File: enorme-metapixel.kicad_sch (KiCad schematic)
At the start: 15 parts, among them J1 VIN, J2 STRIP_0, J3 STRIP_1, J4 STRIP_2, J5 UART, SW1 SW_RESET, SW2 SW_BOOT, U1 BD33FC0FP, U2 ESP32-WROOM-32

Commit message: Rev 2
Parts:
- added D2: Ch.0, ENSADLED:ARGB_0404, symbol Device:LED_ARGB
- added D3: Ch.1, ENSADLED:ARGB_0404, symbol Device:LED_ARGB
- added D4: Ch.2, ENSADLED:ARGB_0404, symbol Device:LED_ARGB
- added H1: M4, MountingHole:MountingHole_4.3mm_M4, symbol Mechanical:MountingHole
- added H2: PEG, MountingHole:MountingHole_3.2mm_M3, symbol Mechanical:MountingHole
- added R22, R23, R24, R25, R26, R27, R28, R29, R30: 3.3k, Resistor_SMD:R_0603_1608Metric, symbol Device:R_Small
- J1: footprint TerminalBlock:TerminalBlock_bornier-2_P5.08mm -> ENSADLED:fiche_bornier-2_P5.08mm
- J2, J3, J4: footprint TerminalBlock:TerminalBlock_bornier-4_P5.08mm -> ENSADLED:fiche-bornier-4_P5.08mm
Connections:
- net VCC: now also D2.1 (A), D3.1 (A), D4.1 (A)
- net ch0_0: now also R23.1
- net ch0_1: now also R22.1
- net ch0_2: now also R24.1
- net ch1_0: now also R26.1
- net ch1_1: now also R25.1
- net ch1_2: now also R27.1
- net ch2_0: now also R29.1
- net ch2_1: now also R28.1
- net ch2_2: now also R30.1
- net ledc6: now reaches U2.12 (IO27)
- net ledc7: now reaches U2.13 (IO14)
- net ledc8: now reaches U2.14 (IO12)
- net ledc3: now reaches U2.26 (IO4)
- net ledc0: now reaches U2.29 (IO5)
- net IO15: no longer names the net of U2.23 (IO15)
- net IO16 renamed ledc4
- net IO17 renamed ledc5
- net IO18 renamed ledc1
- net IO19 renamed ledc2
- net IO21: no longer names the net of U2.33 (IO21)
- net IO22: no longer names the net of U2.36 (IO22)
- net IO23: no longer names the net of U2.37 (IO23)
- net IO25: no longer names the net of U2.10 (IO25)
- new net: D3.2 (RK), R25.2
- new net: D4.4 (BK), R30.2
- new net: D2.4 (BK), R24.2
- new net: D3.4 (BK), R27.2
- new net: D3.3 (GK), R26.2
- new net: D2.2 (RK), R22.2
- new net: D2.3 (GK), R23.2
- new net: D4.2 (RK), R28.2
- new net: D4.3 (GK), R29.2
- no-connect marks 0 -> 8

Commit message: Fix color order
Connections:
- net ch0_0: now also R24.1; no longer R23.1
- net ch0_2: now also R23.1; no longer R24.1
- net ch1_0: now also R27.1; no longer R26.1
- net ch1_2: now also R26.1; no longer R27.1
- net ch2_0: now also R30.1; no longer R29.1
- net ch2_2: now also R29.1; no longer R30.1
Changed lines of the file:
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@@
     (effects (font (size 0.8 0.8)) (justify right bottom))
   )
-  (label "ch0_2" (at 38.1 137.795 0) (fields_autoplaced)
+  (label "ch0_2" (at 38.1 132.715 0) (fields_autoplaced)
     (effects (font (size 0.8 0.8)) (justify left bottom))
   )
@@
     (effects (font (size 0.8 0.8)) (justify left bottom))
   )
-  (label "ch2_0" (at 38.1 178.435 0) (fields_autoplaced)
+  (label "ch2_0" (at 38.1 183.515 0) (fields_autoplaced)
     (effects (font (size 0.8 0.8)) (justify left bottom))
   )
@@
     (effects (font (size 0.8 0.8)) (justify right bottom))
   )
-  (label "ch1_0" (at 38.1 155.575 0) (fields_autoplaced)
+  (label "ch1_0" (at 38.1 160.655 0) (fields_autoplaced)
     (effects (font (size 0.8 0.8)) (justify left bottom))
   )
@@
     (effects (font (size 0.8 0.8)) (justify left bottom))
   )
-  (label "ch1_2" (at 38.1 160.655 0) (fields_autoplaced)
+  (label "ch1_2" (at 38.1 155.575 0) (fields_autoplaced)
     (effects (font (size 0.8 0.8)) (justify left bottom))
   )
-  (label "ch2_2" (at 38.1 183.515 0) (fields_autoplaced)
+  (label "ch2_2" (at 38.1 178.435 0) (fields_autoplaced)
     (effects (font (size 0.8 0.8)) (justify left bottom))
   )
@@
     (effects (font (size 0.8 0.8)) (justify left bottom))
   )
-  (label "ch0_0" (at 38.1 132.715 0) (fields_autoplaced)
+  (label "ch0_0" (at 38.1 137.795 0) (fields_autoplaced)
     (effects (font (size 0.8 0.8)) (justify left bottom))
   )

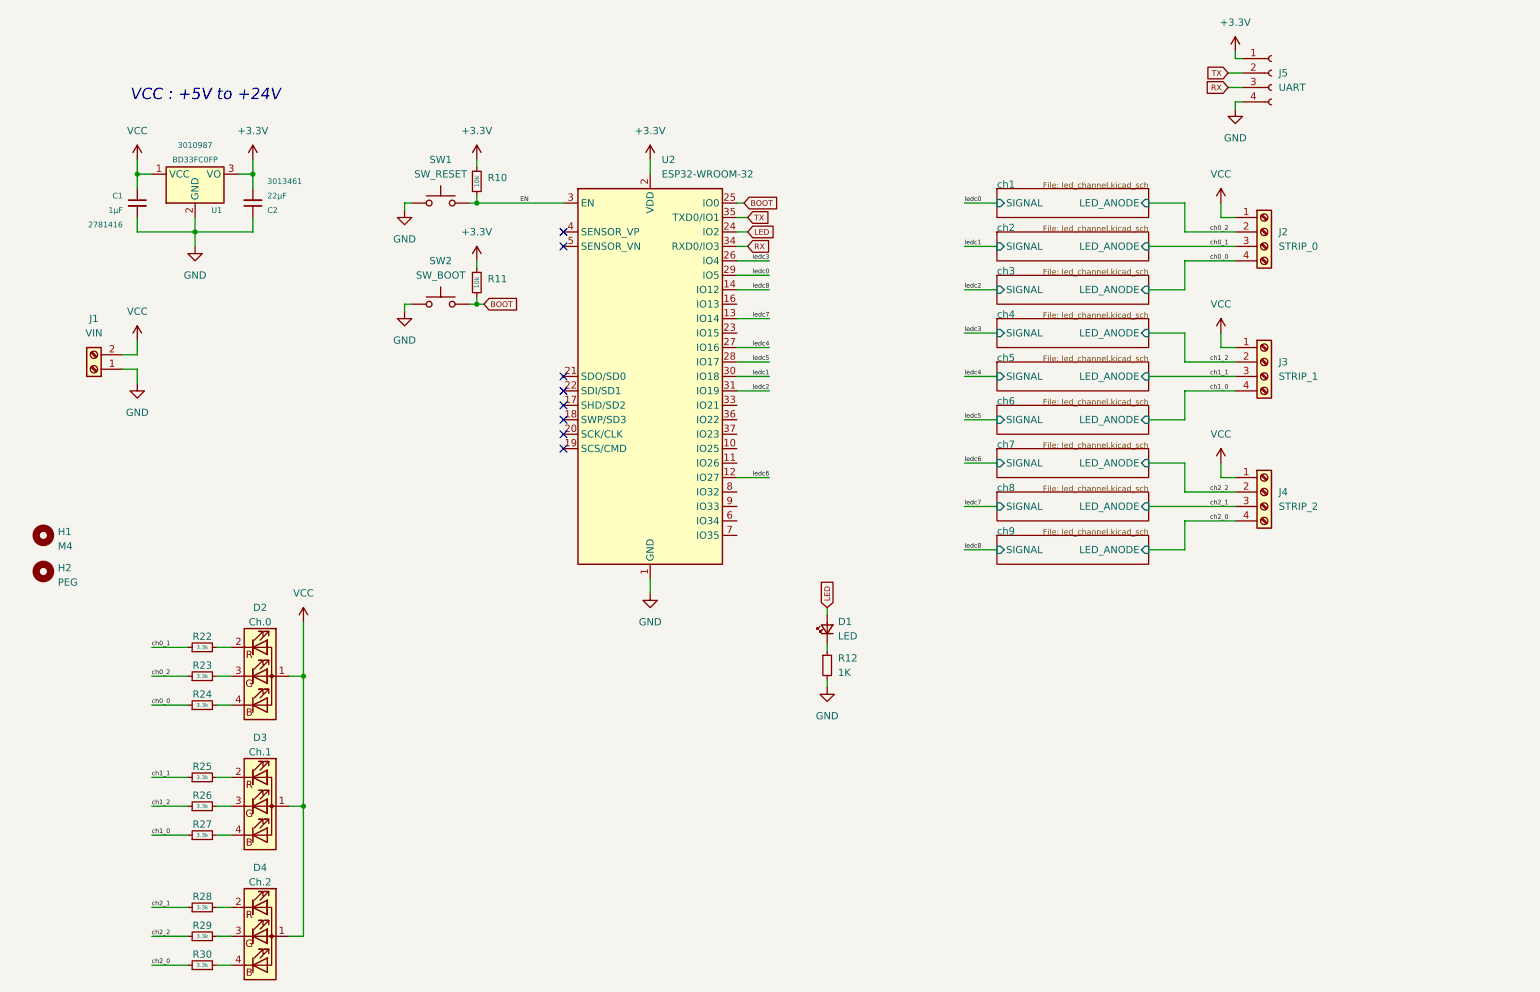
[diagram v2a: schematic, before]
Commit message: Add a second cascaded regulator
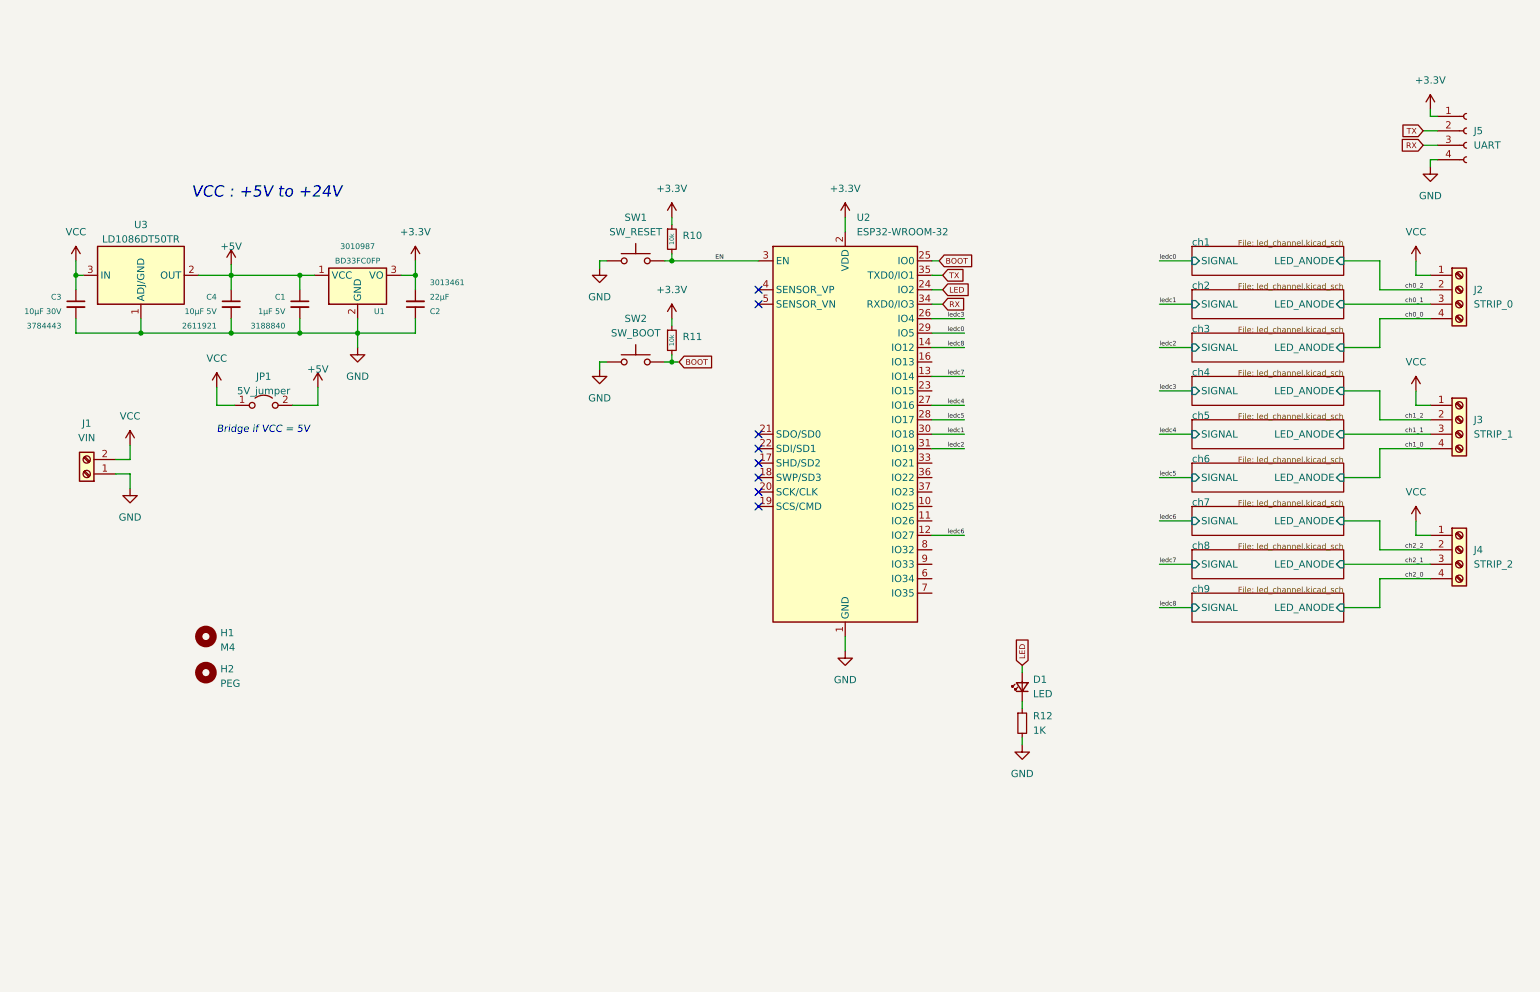
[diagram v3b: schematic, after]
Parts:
- removed D2: Ch.0, ENSADLED:ARGB_0404, symbol Device:LED_ARGB
- removed D3: Ch.1, ENSADLED:ARGB_0404, symbol Device:LED_ARGB
- removed D4: Ch.2, ENSADLED:ARGB_0404, symbol Device:LED_ARGB
- removed R22, R23, R24, R25, R26, R27, R28, R29, R30: 3.3k, Resistor_SMD:R_0603_1608Metric, symbol Device:R_Small
- added C3: 10µF 30V, Capacitor_SMD:C_1206_3216Metric, symbol Device:C_Small
- added C4: 10µF 5V, Capacitor_SMD:C_1206_3216Metric, symbol Device:C_Small
- added JP1: 5V_jumper, symbol Jumper:Jumper_2_Open
- added U3: LD1086DT50TR, Package_TO_SOT_SMD:TO-252-2, symbol Regulator_Linear:LD1086DT50TR
- C1: value 1µF -> 1µF 5V; Farnell 2781416 -> 3188840
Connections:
- net GND: now also C3.2, C4.2, U3.1 (ADJ/GND)
- net VCC: now also C3.1, JP1.1 (A), U3.3 (IN); no longer C1.1, U1.1 (VCC)
- new net +5V: C1.1, C4.1, JP1.2 (B), U1.1 (VCC), U3.2 (OUT)
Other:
- note added: "Bridge if VCC = 5V"
- moved on the sheet: C1, C2, D1, H1, H2, J1, J2, J3, J4, J5, R10, R11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

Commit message: Rev 3
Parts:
- added J6: VIN, ENSADLED:fiche_bornier-2_P5.08mm, symbol Connector:Screw_Terminal_01x02
- C1, C3, C4: footprint Capacitor_SMD:C_1206_3216Metric -> Capacitor_SMD:C_0603_1608Metric
- J2, J3, J4: footprint ENSADLED:fiche-bornier-4_P5.08mm -> ENSADLED:PLUG_Terminal_01x04_2.54mm
- JP1: footprint (none) -> Jumper:SolderJumper-2_P1.3mm_Open_RoundedPad1.0x1.5mm
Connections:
- net GND: now also J6.1 (Pin_1)
- net VCC: now also J6.2 (Pin_2)
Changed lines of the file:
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@@
+    (stroke (width 0) (type default))
+  )
+  (wire (pts (xy 34.29 113.03) (xy 34.29 115.57))
     (stroke (width 0) (type default))
   )
@@
     (stroke (width 0) (type default))
   )
+  (wire (pts (xy 34.29 118.11) (xy 34.29 120.65))
+    (stroke (width 0) (type default))
+  )
   (wire (pts (xy 215.265 113.03) (xy 220.98 113.03))
     (stroke (width 0) (type default))
@@
     (stroke (width 0) (type default))
   )
+  (wire (pts (xy 31.75 115.57) (xy 34.29 115.57))
+    (stroke (width 0) (type default))
+  )
   (wire (pts (xy 128.27 77.47) (xy 129.54 77.47))
     (stroke (width 0) (type default))
@@
   )
   (wire (pts (xy 262.89 41.91) (xy 264.16 41.91))
+    (stroke (width 0) (type default))
+  )
+  (wire (pts (xy 31.75 118.11) (xy 34.29 118.11))
     (stroke (width 0) (type default))
   )
@@
       (effects (font (size 1.27 1.27)) (justify left))
     )
-    (property "Footprint" "ENSADLED:fiche-bornier-4_P5.08mm" (at 267.97 110.49 0)
+    (property "Footprint" "ENSADLED:PLUG_Terminal_01x04_2.54mm" (at 267.97 110.49 0)
       (effects (font (size 1.27 1.27)) hide)
     )
@@
       (effects (font (size 1 1)) (justify right))
     )
-    (property "Footprint" "Capacitor_SMD:C_1206_3216Metric" (at 24.765 67.31 0)
+    (property "Footprint" "Capacitor_SMD:C_0603_1608Metric" (at 24.765 67.31 0)
       (effects (font (size 1.27 1.27)) hide)
     )
@@
       (effects (font (size 1 1)) (justify right))
     )
-    (property "Footprint" "Capacitor_SMD:C_1206_3216Metric" (at 52.07 67.31 0)
+    (property "Footprint" "Capacitor_SMD:C_0603_1608Metric" (at 52.07 67.31 0)
       (effects (font (size 1.27 1.27)) hide)
     )
@@
       (effects (font (size 1.27 1.27)) (justify left))
     )
-    (property "Footprint" "ENSADLED:fiche-bornier-4_P5.08mm" (at 267.97 64.77 0)
+    (property "Footprint" "ENSADLED:PLUG_Terminal_01x04_2.54mm" (at 267.97 64.77 0)
       (effects (font (size 1.27 1.27)) hide)
     )
@@
       (effects (font (size 1 1)) (justify right))
     )
-    (property "Footprint" "Capacitor_SMD:C_1206_3216Metric" (at 64.135 67.31 0)
+    (property "Footprint" "Capacitor_SMD:C_0603_1608Metric" (at 64.135 67.31 0)
       (effects (font (size 1.27 1.27)) hide)
     )
@@
       (effects (font (size 1.27 1.27)))
     )
-    (property "Footprint" "" (at 57.785 85.09 0)
+    (property "Footprint" "Jumper:SolderJumper-2_P1.3mm_Open_RoundedPad1.0x1.5mm" (at 57.785 85.09 0)
       (effects (font (size 1.27 1.27)) hide)
     )
@@
     )
   )
+  (symbol (lib_id "power:VCC") (at 34.29 113.03 0) (unit 1)
+    (in_bom yes) (on_board yes) (dnp no) (fields_autoplaced)
+    (property "Reference" "#PWR05" (at 34.29 116.84 0)
+      (effects (font (size 1.27 1.27)) hide)
+    )
+    (property "Value" "VCC" (at 34.29 107.95 0)
+      (effects (font (size 1.27 1.27)))
+    )
+    (property "Footprint" "" (at 34.29 113.03 0)
+      (effects (font (size 1.27 1.27)) hide)
+    )
+    (property "Datasheet" "" (at 34.29 113.03 0)
+      (effects (font (size 1.27 1.27)) hide)
+    )
+    (pin "1")
+    (instances
+      (project "enorme-metapixel"
+        (path "/46cf7f64-ef08-4474-bf51-0f079d0a1dde"
+          (reference "#PWR05") (unit 1)
+        )
+      )
+    )
+  )
   (symbol (lib_id "Connector:Screw_Terminal_01x04") (at 267.97 87.63 0) (unit 1)
     (in_bom yes) (on_board yes) (dnp no) (fields_autoplaced)
@@
       (effects (font (size 1.27 1.27)) (justify left))
     )
-    (property "Footprint" "ENSADLED:fiche-bornier-4_P5.08mm" (at 267.97 87.63 0)
+    (property "Footprint" "ENSADLED:PLUG_Terminal_01x04_2.54mm" (at 267.97 87.63 0)
       (effects (font (size 1.27 1.27)) hide)
     )
@@
     )
   )
+  (symbol (lib_id "Connector:Screw_Terminal_01x02") (at 26.67 118.11 180) (unit 1)
+    (in_bom yes) (on_board yes) (dnp no) (fields_autoplaced)
+    (property "Reference" "J6" (at 26.67 109.22 0)
+      (effects (font (size 1.27 1.27)))
+    )
+    (property "Value" "VIN" (at 26.67 111.76 0)
+      (effects (font (size 1.27 1.27)))
+    )
+    (property "Footprint" "ENSADLED:fiche_bornier-2_P5.08mm" (at 26.67 118.11 0)
+      (effects (font (size 1.27 1.27)) hide)
+    )
+    (property "Datasheet" "~" (at 26.67 118.11 0)
+      (effects (font (size 1.27 1.27)) hide)
+    )
+    (pin "1")
+    (pin "2")
+    (instances
+      (project "enorme-metapixel"
+        (path "/46cf7f64-ef08-4474-bf51-0f079d0a1dde"
+          (reference "J6") (unit 1)
+        )
+      )
+    )
+  )
   (symbol (lib_id "power:GND") (at 116.84 78.74 0) (unit 1)
     (in_bom yes) (on_board yes) (dnp no) (fields_autoplaced)
@@
         )
       )
+    )
+  )
+  (symbol (lib_id "power:GND") (at 34.29 120.65 0) (unit 1)
+    (in_bom yes) (on_board yes) (dnp no) (fields_autoplaced)
+    (property "Reference" "#PWR06" (at 34.29 127 0)
+      (effects (font (size 1.27 1.27)) hide)
+    )
+    (property "Value" "GND" (at 34.29 125.73 0)
+      (effects (font (size 1.27 1.27)))
+    )
+    (property "Footprint" "" (at 34.29 120.65 0)
+      (effects (font (size 1.27 1.27)) hide)
+    )
+    (property "Datasheet" "" (at 34.29 120.65 0)
+      (effects (font (size 1.27 1.27)) hide)
+    )
+    (pin "1")
+    (instances
+      (project "enorme-metapixel"
+        (path "/46cf7f64-ef08-4474-bf51-0f079d0a1dde"
+          (reference "#PWR06") (unit 1)
+        )
+      )
